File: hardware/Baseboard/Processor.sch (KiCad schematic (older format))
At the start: 25 parts, among them IC1 74HC00, IC10 W65C22, IC2 W65C02, IC3 74HC138, IC4 SYSTEM ROM, IC5 RAM, IC6 W65C22, IC7 W65C51

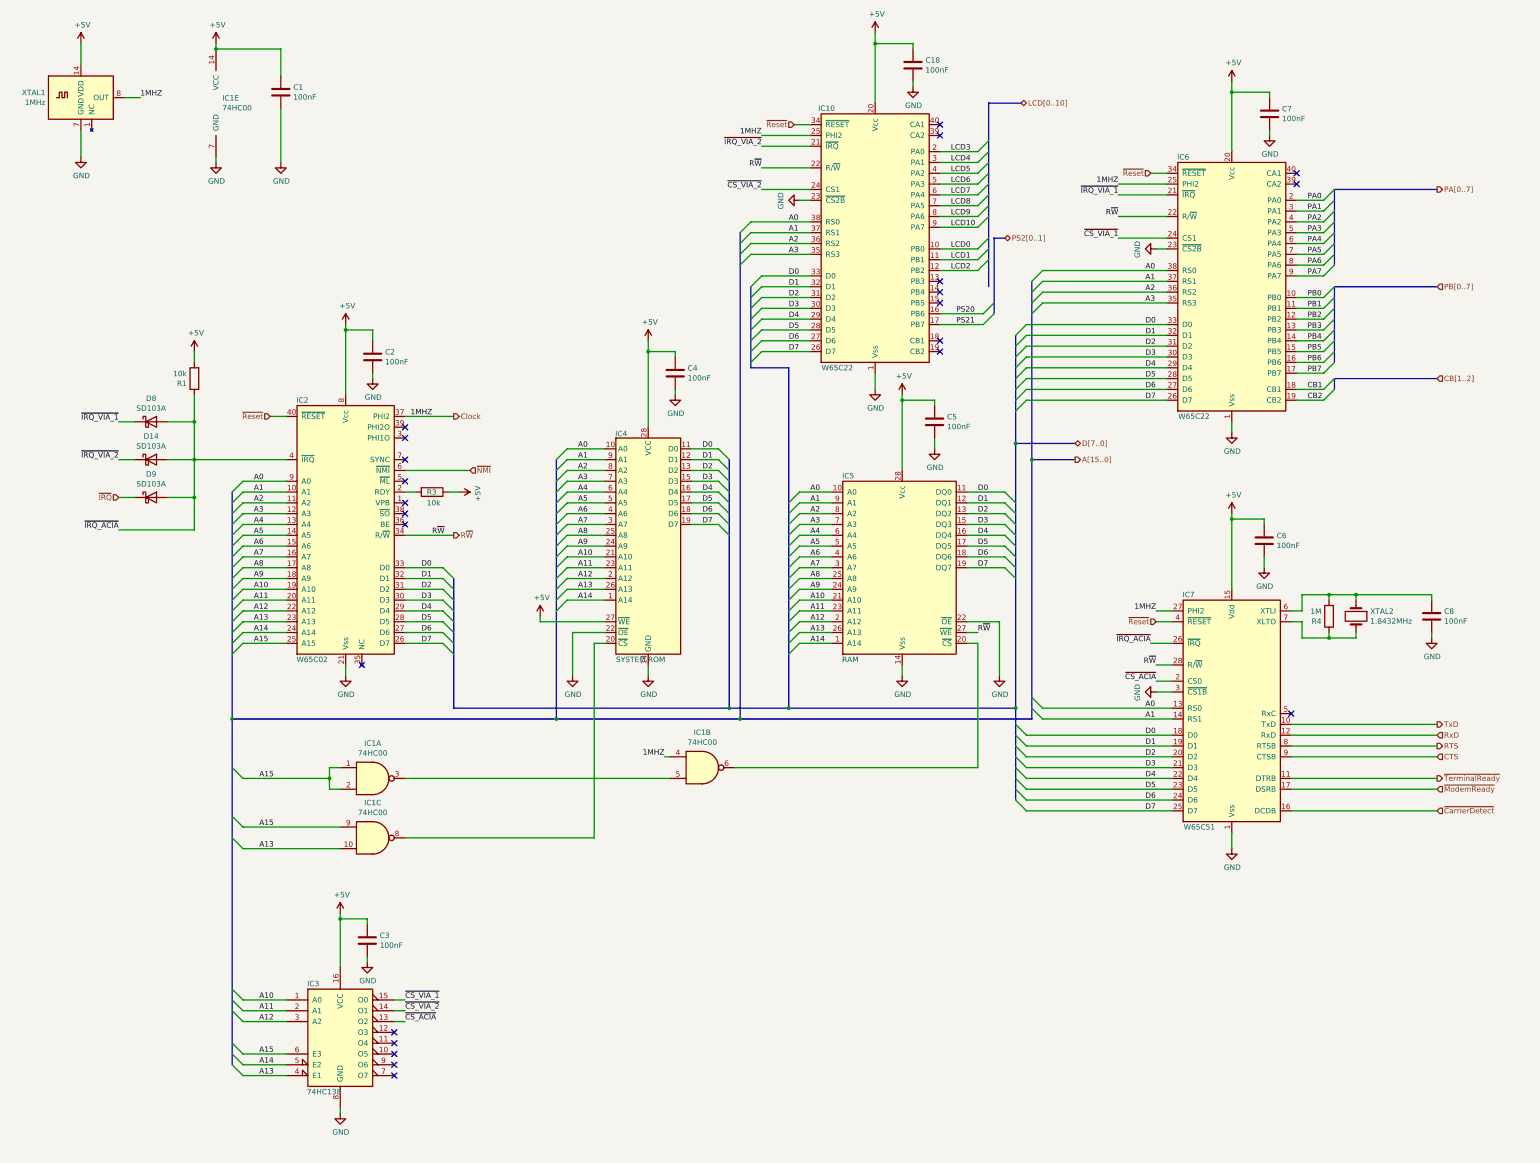
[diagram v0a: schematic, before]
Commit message: Add switch to select between oscillator as clock and manual clock source
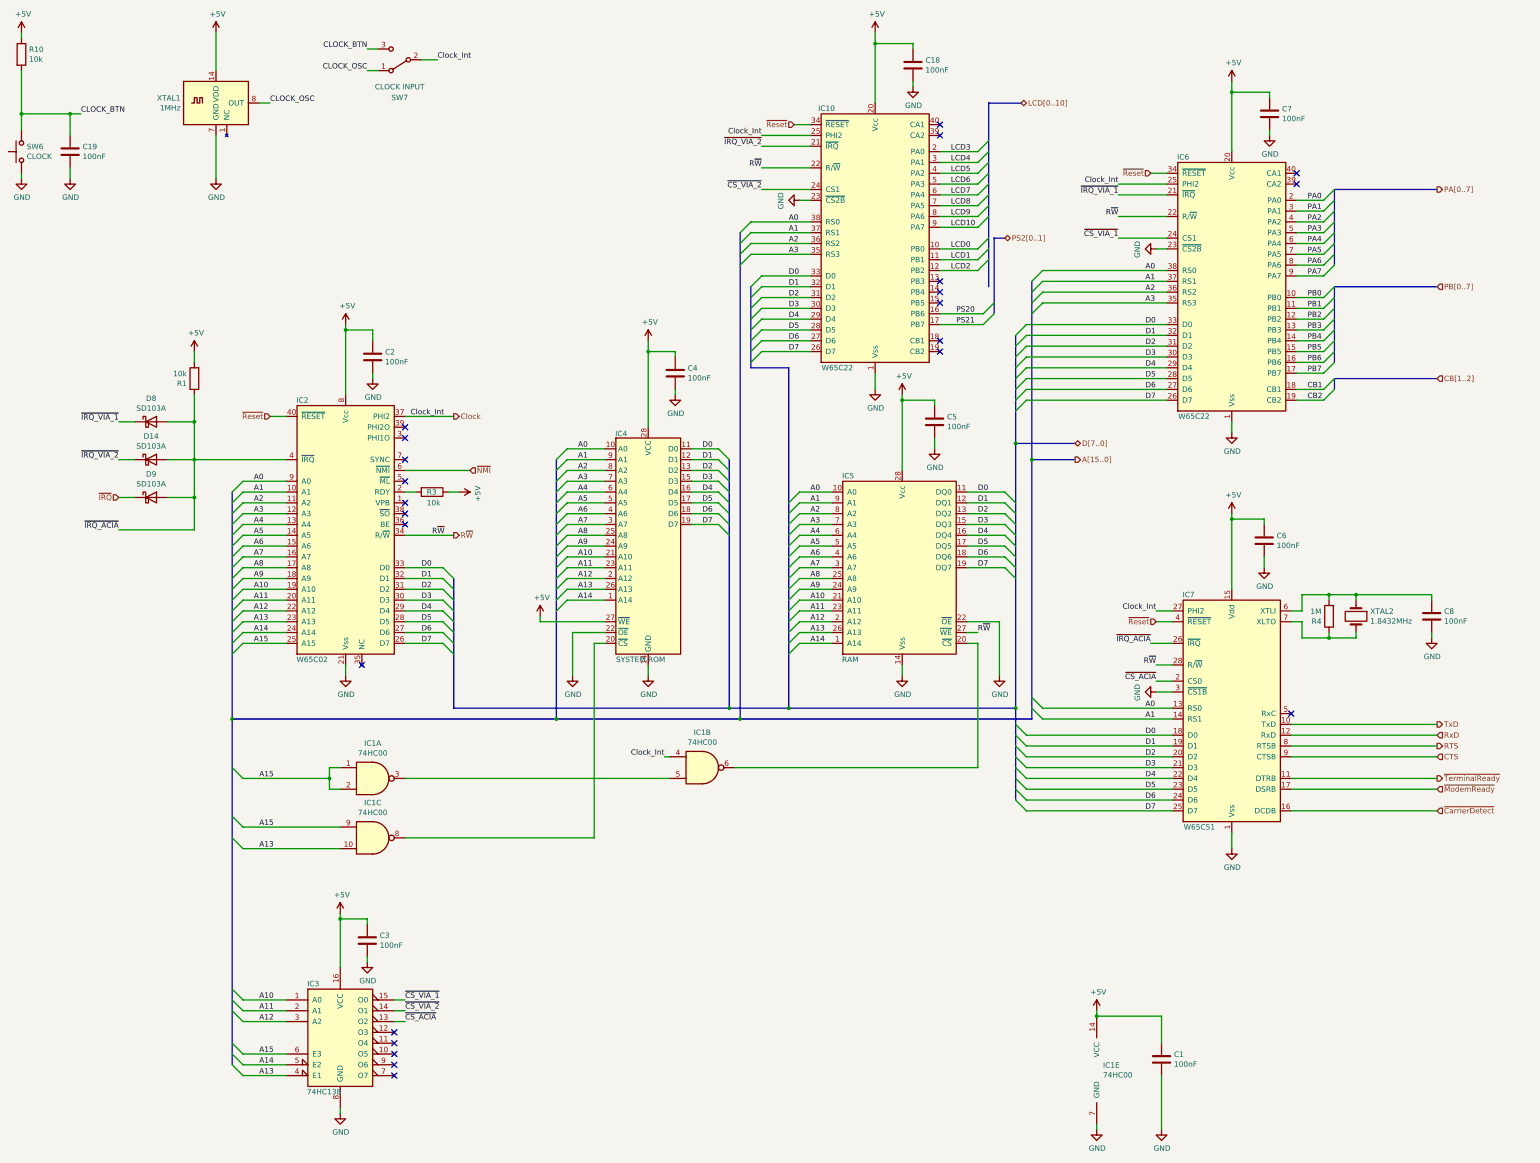
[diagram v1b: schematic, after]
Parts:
- added C19: 100nF, Capacitor_THT:C_Rect_L4.0mm_W2.5mm_P2.50mm, symbol Device:C
- added R10: 10k, Resistor_THT:R_Axial_DIN0207_L6.3mm_D2.5mm_P7.62mm_Horizontal, symbol Device:R
- added SW6: CLOCK, Button_Switch_THT:SW_PUSH_6mm_H4.3mm, symbol Switch:SW_Push
- added SW7: CLOCK INPUT, Button_Switch_THT:SW_E-Switch_EG1271_DPDT, symbol Switch:SW_SPDT
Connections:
- net +5V: now also R10.1
- net Clock: now also SW7.2 (B); no longer XTAL1.8 (OUT)
- net GND: now also C19.2, SW6.1
- new net CLOCK_BTN: C19.1, R10.2, SW6.2, SW7.3 (C)
- new net CLOCK_OSC: SW7.1 (A), XTAL1.8 (OUT)
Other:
- moved on the sheet: C1, IC1E, XTAL1

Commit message: Add switch for clock selection
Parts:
- SW7: footprint Button_Switch_THT:SW_E-Switch_EG1271_DPDT -> Switches:SW_E-Switch_EG1271_DPDT
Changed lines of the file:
@@
 F 0 "SW7" H 4300 1350 50  0000 C CNN
 F 1 "CLOCK INPUT" H 4300 1250 50  0000 C CNN
-F 2 "Button_Switch_THT:SW_E-Switch_EG1271_DPDT" H 4300 1000 50  0001 C CNN
+F 2 "Switches:SW_E-Switch_EG1271_DPDT" H 4300 1000 50  0001 C CNN
 F 3 "https://www.mouser.de/datasheet/2/140/EG-345873.pdf" H 4300 1000 50  0001 C CNN
 F 4 "E-Switch" H 4300 1000 50  0001 C CNN "Mfr."
